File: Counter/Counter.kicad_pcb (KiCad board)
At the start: 2 copper layers, 99.6 x 59.9 mm, 40 parts, among them J1 Conn_01x16, J2 Conn_01x16, J3 Conn_01x16, J4 Conn_01x16, U1 74LS00, U10 74LS245, U2 74LS04, U4 74LS161, U5 74LS161, U6 74LS161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

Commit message: Fixed floating inputs; improved power; added parts list; replaced JK latches
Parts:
- RN1, RN2: value 100k -> 1k
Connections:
- U1 pad 10: (no net) -> GND
- U1 pad 11: (no net) -> Net-(U1-Pad11)
- U1 pad 12: (no net) -> GND
- U1 pad 13: (no net) -> GND
- U1 pad 8: (no net) -> Net-(U1-Pad8)
- U1 pad 9: (no net) -> GND
- U2 pad 10: (no net) -> Net-(U2-Pad10)
- U2 pad 11: (no net) -> GND
- U2 pad 12: (no net) -> Net-(U2-Pad12)
- U2 pad 13: (no net) -> GND
- U2 pad 8: (no net) -> Net-(U2-Pad8)
- U2 pad 9: (no net) -> GND
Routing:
- net GND: track 316.2 -> 348.5 mm

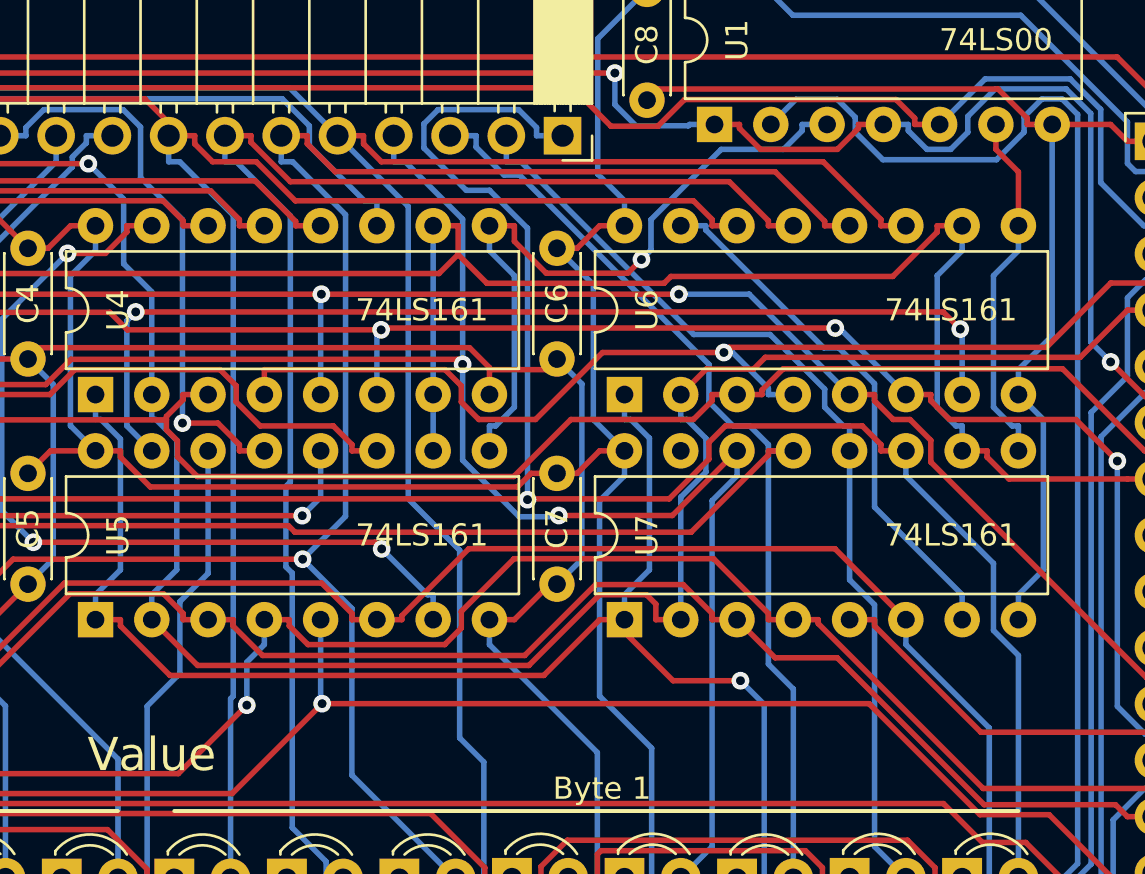
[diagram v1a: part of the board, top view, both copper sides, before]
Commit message: Fix reversed headers on ALU, and counting issues on counter (CET / CEP connections)
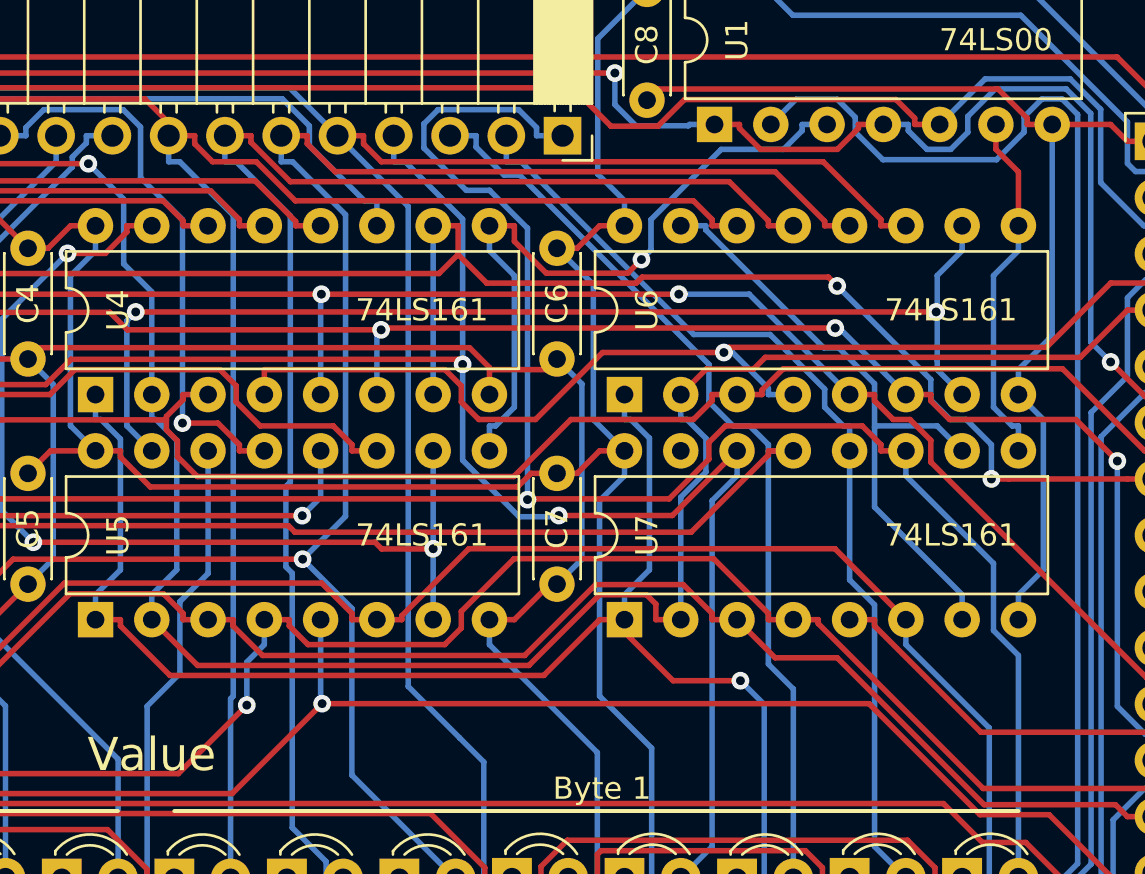
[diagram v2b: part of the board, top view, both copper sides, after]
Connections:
- U5 pad 10: SIG0 -> Net-(U4-Pad15)
- U6 pad 10: SIG0 -> Net-(U5-Pad15)
- U7 pad 10: SIG0 -> Net-(U6-Pad15)
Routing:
- net SIG0: track 126.3 -> 116.0 mm, vias 0 -> 2
- net Net-(U4-Pad15): track 39.5 -> 45.1 mm
- net Net-(U6-Pad15): track 24.1 -> 28.5 mm
- net Net-(U5-Pad15): track 47.4 -> 51.6 mm

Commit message: Update all boards to r3, and update revision log and gitignore
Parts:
- added HOLE1: MountingHole_2.2mm_M2_DIN965_Pad, MountingHole:MountingHole_2.2mm_M2_DIN965_Pad, F.Cu at (35.6, 38.1)
- added HOLE2: MountingHole_2.2mm_M2_DIN965_Pad, MountingHole:MountingHole_2.2mm_M2_DIN965_Pad, F.Cu at (127.0, 38.1)
- added HOLE3: MountingHole_2.2mm_M2_DIN965_Pad, MountingHole:MountingHole_2.2mm_M2_DIN965_Pad, F.Cu at (35.6, 89.9)
- added HOLE4: MountingHole_2.2mm_M2_DIN965_Pad, MountingHole:MountingHole_2.2mm_M2_DIN965_Pad, F.Cu at (127.0, 89.9)
- U1: value 74LS00 -> 74HC00
- U10: value 74LS245 -> 74HC245
- U2: value 74LS04 -> 74HC04
- U4, U5, U6, U7: value 74LS161 -> 74HC161
- U8, U9: value 74LS157 -> 74HC157
- moved RN2 47.0 mm to (95.0, 62.7)
- moved U5 45.9 mm to (40.6, 91.4)
- moved RN1 42.9 mm to (95.0, 66.8)
- moved C5 36.4 mm to (41.9, 72.1), turned to 0 degrees
- moved C9 1.02 mm to (103.6, 90.4)
- moved U2 1.02 mm to (106.7, 91.4)
- moved C8 0.51 mm to (103.6, 38.1)
- moved U1 0.51 mm to (106.7, 44.2)
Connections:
- net ~RESET renamed ~{RESET}
- net ~SIG1 renamed ~{SIG1}
- net ~SIG_IN_0 renamed ~{SIG_IN_0}
- net ~SIG_IN_1 renamed ~{SIG_IN_1}
- D1 pad 2: A0 -> A15
- D10 pad 2: A9 -> A6
- D11 pad 2: A10 -> A5
- D12 pad 2: A11 -> A4
- D13 pad 2: A12 -> A3
- D14 pad 2: A13 -> A2
- D15 pad 2: A14 -> A1
- D16 pad 2: A15 -> A0
- D2 pad 2: A1 -> A14
- D3 pad 2: A2 -> A13
- D4 pad 2: A3 -> A12
- D5 pad 2: A4 -> A11
- D6 pad 2: A5 -> A10
- D7 pad 2: A6 -> A9
- D8 pad 2: A7 -> A8
- D9 pad 2: A8 -> A7
- U1 pad 11: Net-(U1-Pad11) -> unconnected-(U1-Pad11)
- U1 pad 8: Net-(U1-Pad8) -> unconnected-(U1-Pad8)
- U2 pad 10: Net-(U2-Pad10) -> CLOCK_BUF
- U2 pad 11: GND -> Net-(U2-Pad11)
- U2 pad 12: Net-(U2-Pad12) -> Net-(U2-Pad11)
- U2 pad 13: GND -> CLOCK
- U2 pad 8: Net-(U2-Pad8) -> unconnected-(U2-Pad8)
- U4 pad 2: CLOCK -> CLOCK_BUF
- U5 pad 2: CLOCK -> CLOCK_BUF
- U6 pad 2: CLOCK -> CLOCK_BUF
- U7 pad 15: Net-(U7-Pad15) -> unconnected-(U7-TC-Pad15)
- U7 pad 2: CLOCK -> CLOCK_BUF
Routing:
- net CLOCK_BUF: track 0.00 -> 139.9 mm, vias 0 -> 2
- net ~{SIG_IN_0}: track 31.5 -> 164.2 mm
- net BUS1: track 216.8 -> 109.6 mm
- net Net-(U5-TC): track 51.6 -> 143.7 mm
- net BUS2: track 146.3 -> 227.1 mm, vias 4 -> 1
- net A0: track 93.0 -> 169.7 mm
- net A1: track 88.8 -> 160.3 mm, vias 0 -> 3
- net ~{RESET}: track 84.1 -> 140.4 mm, vias 1 -> 2
- net BUS0: track 120.4 -> 173.0 mm, vias 0 -> 3
- net Net-(D12-K): track 76.2 -> 26.6 mm
- net A2: track 84.3 -> 130.1 mm, vias 0 -> 2
- net BUS4: track 123.5 -> 167.2 mm, vias 0 -> 1
- net Net-(D14-K): track 70.5 -> 28.1 mm, vias 1 -> 0
- net Net-(D13-K): track 69.6 -> 28.0 mm, vias 1 -> 0
- net Net-(D15-K): track 70.0 -> 30.2 mm
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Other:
- net class Default removed
